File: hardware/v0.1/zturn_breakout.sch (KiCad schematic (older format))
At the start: 4 parts, among them J1 Z-Turn CN1, J2 Z-Turn JTAG, J3 Z-Turn CN2, J4 HS3-JTAG

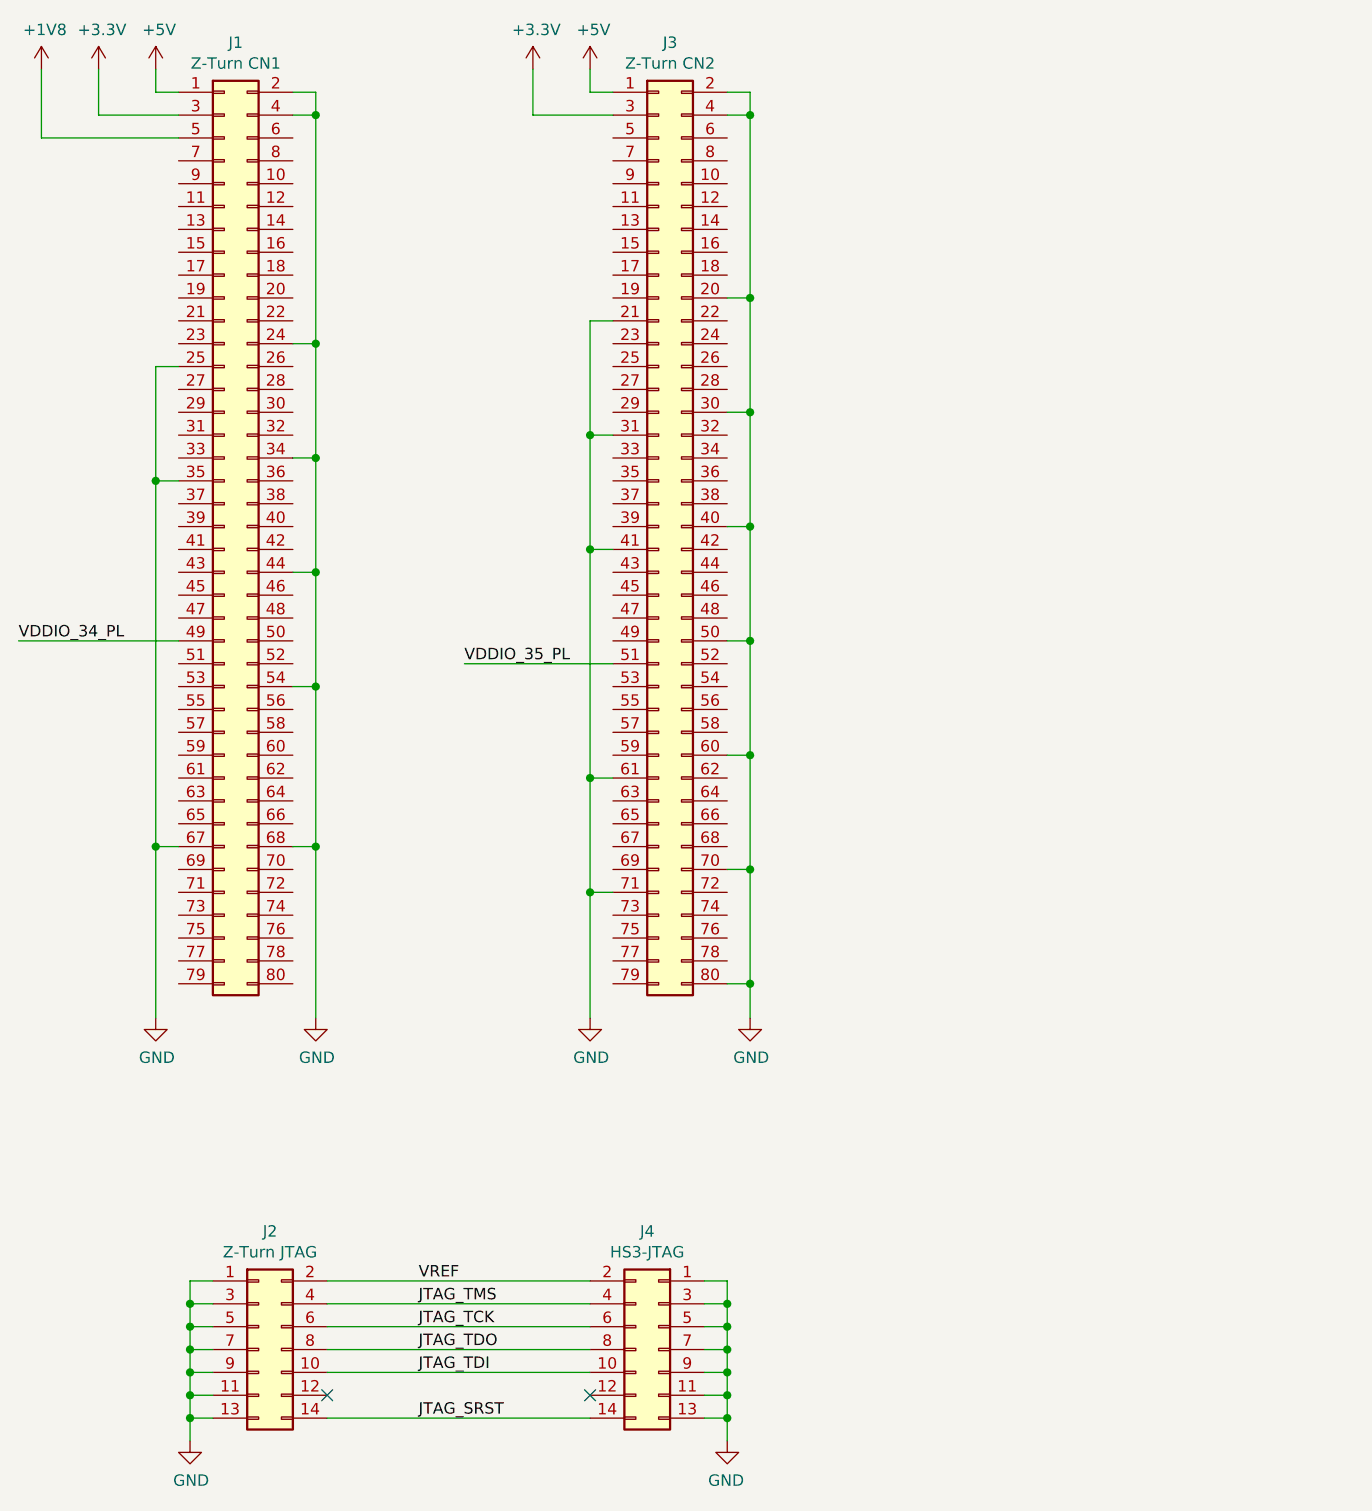
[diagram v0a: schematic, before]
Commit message: Cleaned up v0.1 and began v1.0 schematic
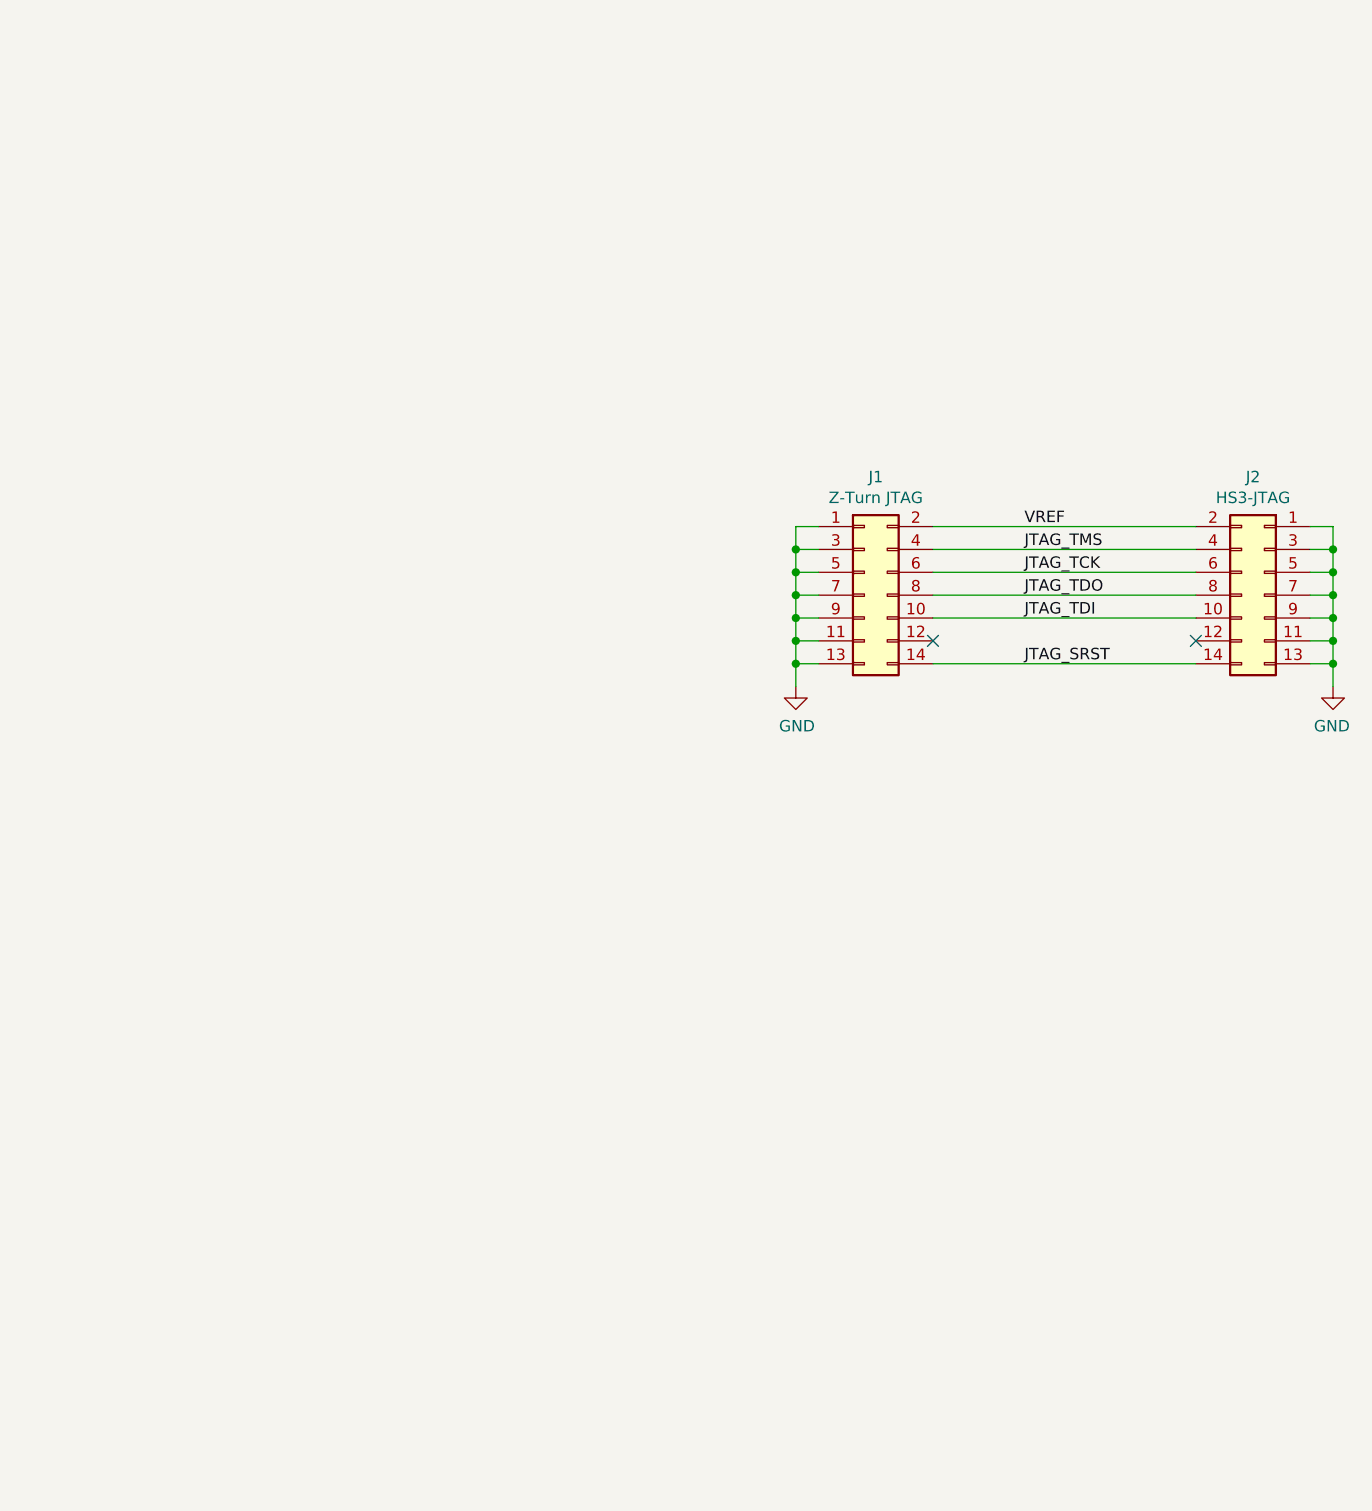
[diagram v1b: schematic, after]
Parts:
- removed J1: Z-Turn CN1, Connector_PinHeader_1.27mm:PinHeader_2x40_P1.27mm_Vertical, symbol Connector_Generic:Conn_02x40_Odd_Even
- removed J3: Z-Turn CN2, Connector_PinHeader_1.27mm:PinHeader_2x40_P1.27mm_Vertical, symbol Connector_Generic:Conn_02x40_Odd_Even
- renumbered J2 to J1, J4 to J2
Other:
- moved on the sheet: J1, J2
